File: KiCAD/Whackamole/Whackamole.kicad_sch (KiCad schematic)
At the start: 53 parts, among them SW1 SW_Push, SW2 SW_Push, SW3 SW_Push, SW4 SW_Push, SW5 SW_Push, SW6 SW_Push, SW7 SW_Push, SW8 SW_Push, SW9 SW_Push, U1 HDSP-7401, U2 CD4026BE, U3 CD4026BE, U4 HDSP-7401

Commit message: Grosse MàJ !! IMPORTANT DE LIRE LE RAPPORT LaTeX
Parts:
- added D10: LED_penalty, symbol Device:LED
- added R22: R, symbol Device:R
- added StartButton: SW_Push, symbol Switch:SW_Push
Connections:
- net GND: now also D10.1 (K), R22.1
- net VCC: now also StartButton.2
- net at 5M160ZE64C1.14 (GPIO20): now also D10.2 (A)
- net at 5M160ZE64C1.15 (GPIO21): now also R22.2, StartButton.1

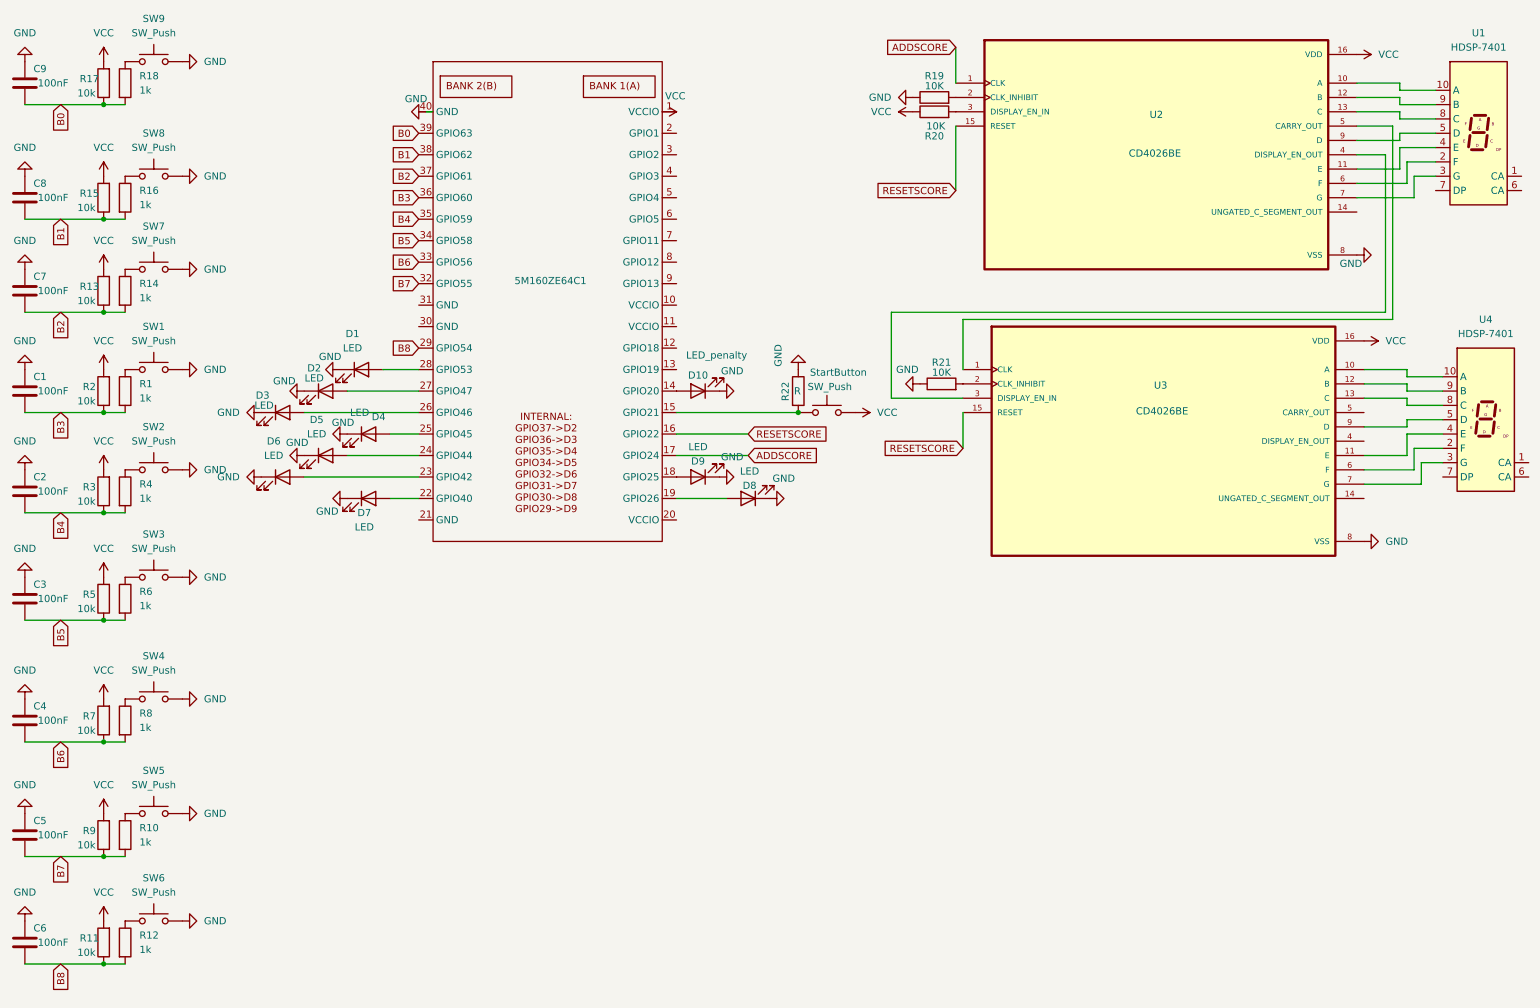
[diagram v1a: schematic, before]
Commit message: Changé commentaires en Anglais
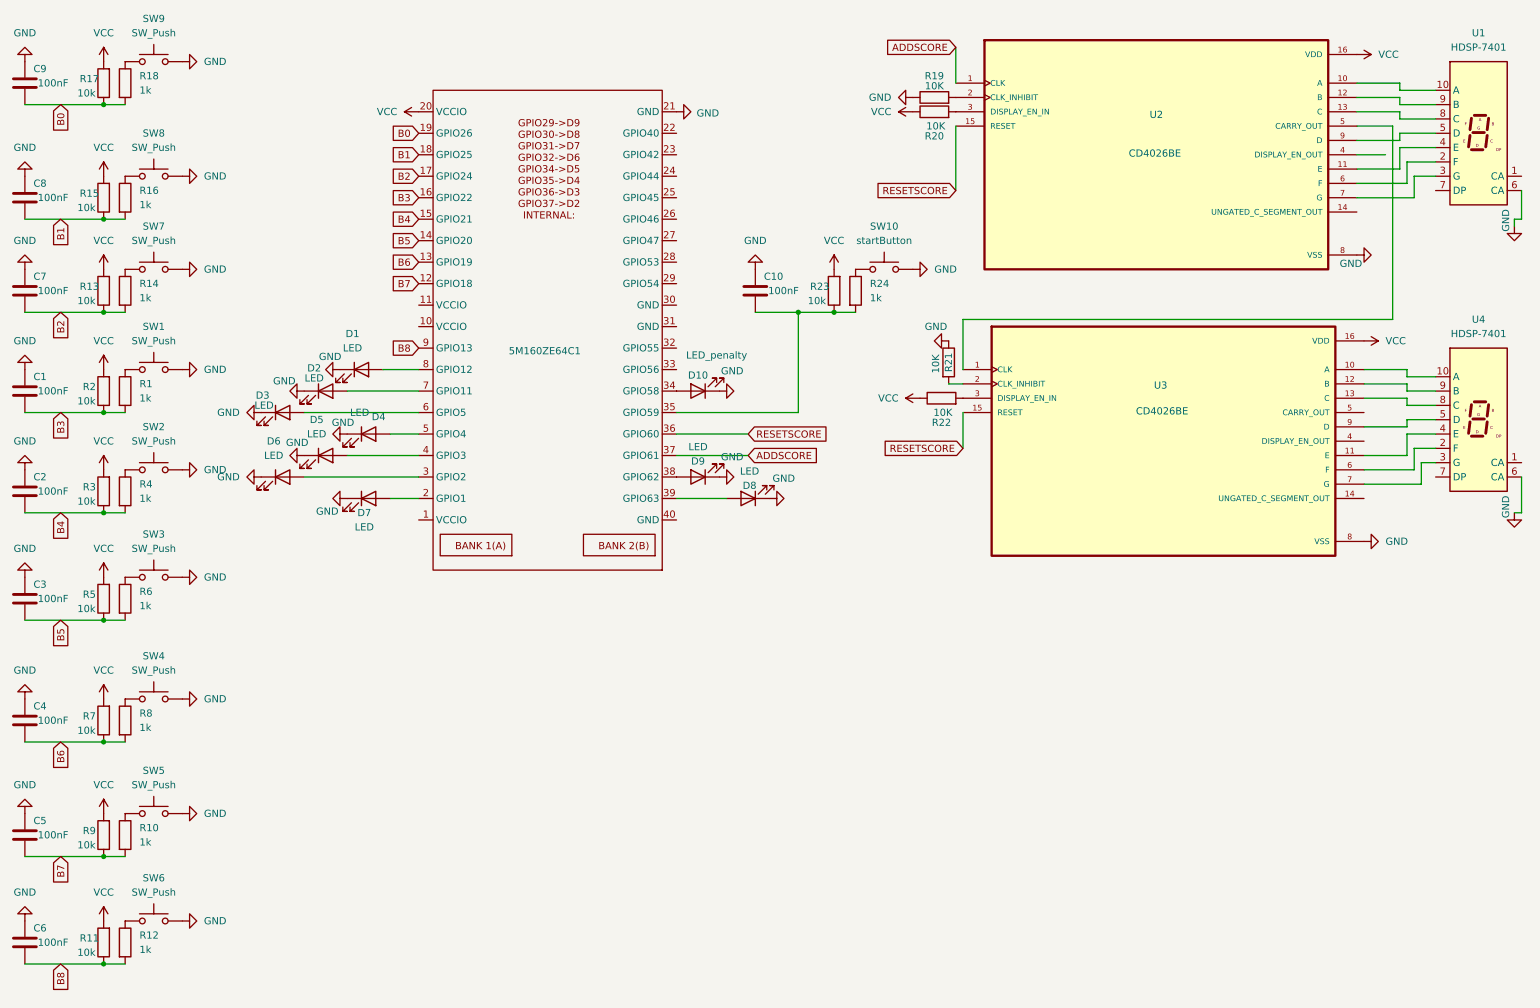
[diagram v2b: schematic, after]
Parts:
- removed StartButton: SW_Push, symbol Switch:SW_Push
- added C10: 100nF, symbol Device:C
- added R23: 10k, symbol Device:R
- added R24: 1k, symbol Device:R
- added SW10: startButton, symbol Switch:SW_Push
- 5M160ZE64C1: value ~ -> (none)
- R22: value R -> 10K
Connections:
- net ADDSCORE: now also 5M160ZE64C1.37 (GPIO61); no longer 5M160ZE64C1.17 (GPIO24)
- net B0: now also 5M160ZE64C1.19 (GPIO26); no longer 5M160ZE64C1.39 (GPIO63)
- net B1: now also 5M160ZE64C1.18 (GPIO25); no longer 5M160ZE64C1.38 (GPIO62)
- net B2: now also 5M160ZE64C1.17 (GPIO24); no longer 5M160ZE64C1.37 (GPIO61)
- net B3: now also 5M160ZE64C1.16 (GPIO22); no longer 5M160ZE64C1.36 (GPIO60)
- net B4: now also 5M160ZE64C1.15 (GPIO21); no longer 5M160ZE64C1.35 (GPIO59)
- net B5: now also 5M160ZE64C1.14 (GPIO20); no longer 5M160ZE64C1.34 (GPIO58)
- net B6: now also 5M160ZE64C1.13 (GPIO19); no longer 5M160ZE64C1.33 (GPIO56)
- net B7: now also 5M160ZE64C1.12 (GPIO18); no longer 5M160ZE64C1.32 (GPIO55)
- net B8: now also 5M160ZE64C1.9 (GPIO13); no longer 5M160ZE64C1.29 (GPIO54)
- net GND: now also 5M160ZE64C1.21 (GND), U1.6 (CA), U4.6 (CA), C10.2, SW10.2; no longer R22.1
- net RESETSCORE: now also 5M160ZE64C1.36 (GPIO60); no longer 5M160ZE64C1.16 (GPIO22)
- net VCC: now also 5M160ZE64C1.20 (VCCIO), R22.1, R23.2
- net at D1.2 (A): now also 5M160ZE64C1.8 (GPIO12); no longer 5M160ZE64C1.28 (GPIO53)
- net at D10.2 (A): now also 5M160ZE64C1.34 (GPIO58); no longer 5M160ZE64C1.14 (GPIO20)
- net at D5.2 (A): now also 5M160ZE64C1.4 (GPIO3); no longer 5M160ZE64C1.24 (GPIO44)
- net at U2.4 (DISPLAY_EN_OUT): no longer U3.3 (DISPLAY_EN_IN)
- net at R22.2: now also U3.3 (DISPLAY_EN_IN); no longer 5M160ZE64C1.15 (GPIO21)
- net at D3.2 (A): now also 5M160ZE64C1.6 (GPIO5); no longer 5M160ZE64C1.26 (GPIO46)
- net at D4.2 (A): now also 5M160ZE64C1.5 (GPIO4); no longer 5M160ZE64C1.25 (GPIO45)
- net at D8.2 (A): now also 5M160ZE64C1.39 (GPIO63); no longer 5M160ZE64C1.19 (GPIO26)
- net at D7.2 (A): now also 5M160ZE64C1.2 (GPIO1); no longer 5M160ZE64C1.22 (GPIO40)
- net at D6.2 (A): now also 5M160ZE64C1.3 (GPIO2); no longer 5M160ZE64C1.23 (GPIO42)
- net at D9.2 (A): now also 5M160ZE64C1.38 (GPIO62); no longer 5M160ZE64C1.18 (GPIO25)
- net at 5M160ZE64C1.27 (GPIO47): no longer D2.2 (A)
- net at 5M160ZE64C1.7 (GPIO11): now also D2.2 (A)
- new net: 5M160ZE64C1.35 (GPIO59), C10.1, R23.1, R24.2
- new net: R24.1, SW10.1
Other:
- moved on the sheet: 5M160ZE64C1, R21, U4
